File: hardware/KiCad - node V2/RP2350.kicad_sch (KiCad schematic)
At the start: 91 parts, among them J3 USB_C_Receptacle_USB2.0_14P, SW1 BOOTSEL, U1 RP2350A, U2 THVD1450D, U3 ADXL355BEZ, U4 TPS2121RUXR, U5 USBLC6-2SC6, U6 TLV75733PDBV, U7 W25Q128JVS, U8 TPS7A20xxxDBV

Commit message: hardware: 3v3_dig, 1vcore
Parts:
- C19, C20, C21, C22, C25: footprint Capacitor_SMD:C_0603_1608Metric -> Capacitor_SMD:C_0402_1005Metric
- C23, C26: footprint Capacitor_SMD:C_0805_2012Metric -> Capacitor_SMD:C_0603_1608Metric
- R17: footprint Resistor_SMD:R_0201_0603Metric -> Resistor_SMD:R_0402_1005Metric
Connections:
- net USB_VBUS: now also J3.A4 (VBUS), J3.A9 (VBUS), J3.B4 (VBUS)
- net at U2.1 (RO): now also U1.29 (GPIO18)
- net at U2.4 (DI): now also U1.31 (GPIO19)
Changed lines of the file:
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@@
 	)
 	(junction
+		(at 186.69 241.3)
+		(diameter 0)
+		(color 0 0 0 0)
+	)
+	(junction
 		(at 137.16 228.6)
 		(diameter 0)
@@
 	)
 	(junction
+		(at 173.99 232.41)
+		(diameter 0)
+		(color 0 0 0 0)
+	)
+	(junction
 		(at 100.33 113.03)
 		(diameter 0)
@@
 	)
 	(junction
+		(at 173.99 241.3)
+		(diameter 0)
+		(color 0 0 0 0)
+	)
+	(junction
 		(at 46.99 237.49)
 		(diameter 0)
@@
 	(wire
 		(pts
+			(xy 186.69 255.27) (xy 186.69 241.3)
+		)
+		(stroke
+			(width 0)
+			(type default)
+		)
+	)
+	(wire
+		(pts
 			(xy 196.85 31.75) (xy 196.85 34.29)
 		)
@@
 	(wire
 		(pts
+			(xy 214.63 78.74) (xy 214.63 88.9)
+		)
+		(stroke
+			(width 0)
+			(type default)
+		)
+	)
+	(wire
+		(pts
 			(xy 201.93 40.64) (xy 198.12 40.64)
 		)
@@
 	(wire
 		(pts
+			(xy 186.69 232.41) (xy 186.69 241.3)
+		)
+		(stroke
+			(width 0)
+			(type default)
+		)
+	)
+	(wire
+		(pts
 			(xy 123.19 76.2) (xy 121.92 76.2)
 		)
@@
 	(wire
 		(pts
-			(xy 121.92 72.39) (xy 168.91 72.39)
+			(xy 121.92 72.39) (xy 217.17 72.39)
 		)
 		(stroke
@@
 	(wire
 		(pts
+			(xy 173.99 232.41) (xy 173.99 241.3)
+		)
+		(stroke
+			(width 0)
+			(type default)
+		)
+	)
+	(wire
+		(pts
 			(xy 52.07 142.24) (xy 52.07 157.48)
 		)
@@
 	(wire
 		(pts
+			(xy 217.17 72.39) (xy 217.17 88.9)
+		)
+		(stroke
+			(width 0)
+			(type default)
+		)
+	)
+	(wire
+		(pts
 			(xy 100.33 133.35) (xy 100.33 135.89)
 		)
@@
 	(wire
 		(pts
-			(xy 121.92 78.74) (xy 171.45 78.74)
+			(xy 121.92 78.74) (xy 214.63 78.74)
 		)
 		(stroke
@@
 	(wire
 		(pts
+			(xy 173.99 241.3) (xy 173.99 255.27)
+		)
+		(stroke
+			(width 0)
+			(type default)
+		)
+	)
+	(wire
+		(pts
 			(xy 181.61 247.65) (xy 181.61 255.27)
 		)
@@
 	(wire
 		(pts
+			(xy 186.69 241.3) (xy 173.99 241.3)
+		)
+		(stroke
+			(width 0)
+			(type default)
+		)
+	)
+	(wire
+		(pts
 			(xy 209.55 142.24) (xy 255.27 142.24)
 		)
@@
 			)
 		)
-		(property "Footprint" "Capacitor_SMD:C_0603_1608Metric"
+		(property "Footprint" "Capacitor_SMD:C_0402_1005Metric"
 			(at 153.67 127 0)
 			(hide yes)
@@
 			)
 		)
-		(property "Footprint" "Capacitor_SMD:C_0805_2012Metric"
+		(property "Footprint" "Capacitor_SMD:C_0603_1608Metric"
 			(at 134.62 114.3 0)
 			(hide yes)
@@
 			)
 		)
-		(property "Footprint" "Capacitor_SMD:C_0603_1608Metric"
+		(property "Footprint" "Capacitor_SMD:C_0402_1005Metric"
 			(at 158.75 129.54 0)
 			(hide yes)
@@
 			)
 		)
-		(property "Footprint" "Capacitor_SMD:C_0603_1608Metric"
+		(property "Footprint" "Capacitor_SMD:C_0402_1005Metric"
 			(at 154.94 87.63 0)
 			(hide yes)
@@
 			)
 		)
-		(property "Footprint" "Capacitor_SMD:C_0603_1608Metric"
+		(property "Footprint" "Capacitor_SMD:C_0402_1005Metric"
 			(at 142.24 119.38 0)
 			(hide yes)
@@
 			)
 		)
-		(property "Footprint" "Capacitor_SMD:C_0805_2012Metric"
+		(property "Footprint" "Capacitor_SMD:C_0603_1608Metric"
 			(at 148.59 87.63 0)
 			(hide yes)
@@
 			)
 		)
-		(property "Footprint" "Resistor_SMD:R_0201_0603Metric"
+		(property "Footprint" "Resistor_SMD:R_0402_1005Metric"
 			(at 144.78 135.89 0)
 			(hide yes)
@@
 			)
 		)
-		(property "Footprint" "Capacitor_SMD:C_0603_1608Metric"
+		(property "Footprint" "Capacitor_SMD:C_0402_1005Metric"
 			(at 149.86 121.92 0)
 			(hide yes)

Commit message: hardware: new layout
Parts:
- removed R25, R26, R28, R29: 33ohm, Resistor_SMD:R_0603_1608Metric, symbol Device:R_Small
- C30, C34, C35, C37: footprint Capacitor_SMD:C_0603_1608Metric -> Capacitor_SMD:C_0402_1005Metric
- C36: footprint Capacitor_SMD:C_0805_2012Metric -> Capacitor_SMD:C_0603_1608Metric
- R23, R24, R27: footprint Resistor_SMD:R_0603_1608Metric -> Resistor_SMD:R_0402_1005Metric
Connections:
- net GND: now also J_OUT1.2 (GND)
- net SHIELD: now also J_OUT1.5 (SHIELD)
- net at U2.1 (RO): now also U1.27 (GPIO16); no longer U1.29 (GPIO18)
- net at R22.2, U2.2 (~{RE}), U2.3 (DE): now also U1.29 (GPIO18); no longer U1.4 (GPIO2)
- net at U2.4 (DI): now also U1.28 (GPIO17); no longer U1.31 (GPIO19)
- net ADXL_MISO: now reaches U3.4 (MISO/ASEL)
- net ADXL_MISO: now also U1.12 (GPIO8)
- net ADXL_CS: now reaches R27.2, U3.1 (*CS/SCL)
- net ADXL_CS: now also U1.13 (GPIO9)
- net ADXL_INT1: now reaches U3.12 (INT1)
- net ADXL_INT1: now also U1.18 (GPIO14); no longer U1.17 (GPIO13)
- net ADXL_INT2: now reaches U3.13 (INT2)
- net ADXL_INT2: now also U1.17 (GPIO13); no longer U1.18 (GPIO14)
- net ADXL_DRDY: now reaches U1.16 (GPIO12), U3.14 (DRDY)
- net ADXL_SCLK: now reaches U3.2 (SCLK/VSSIO)
- net ADXL_SCLK: now also U1.14 (GPIO10)
- net ADXL_MOSI: now reaches U3.3 (MOSI/SDA)
- net ADXL_MOSI: now also U1.15 (GPIO11)
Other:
- moved on the sheet: R22, R27

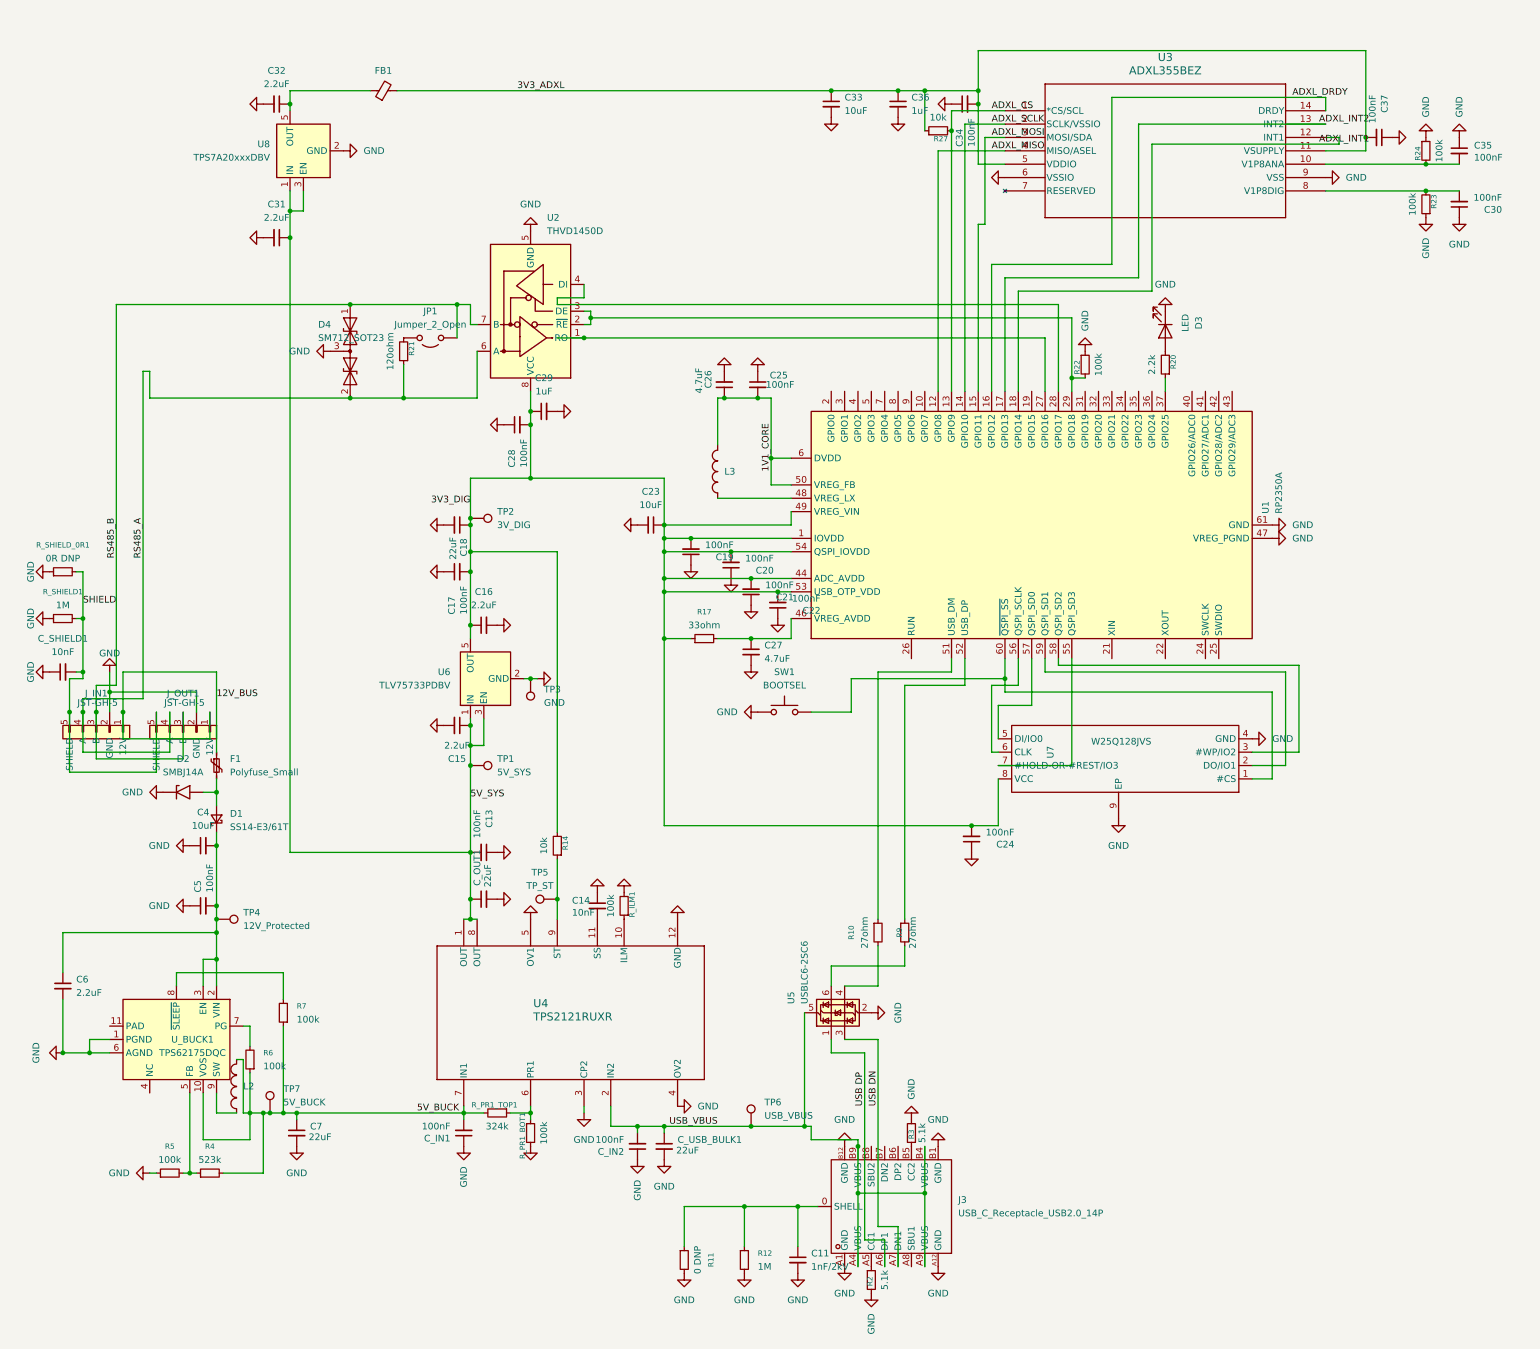
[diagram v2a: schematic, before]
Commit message: hardware: ERC fixes, PWR_FLAG, and net labels
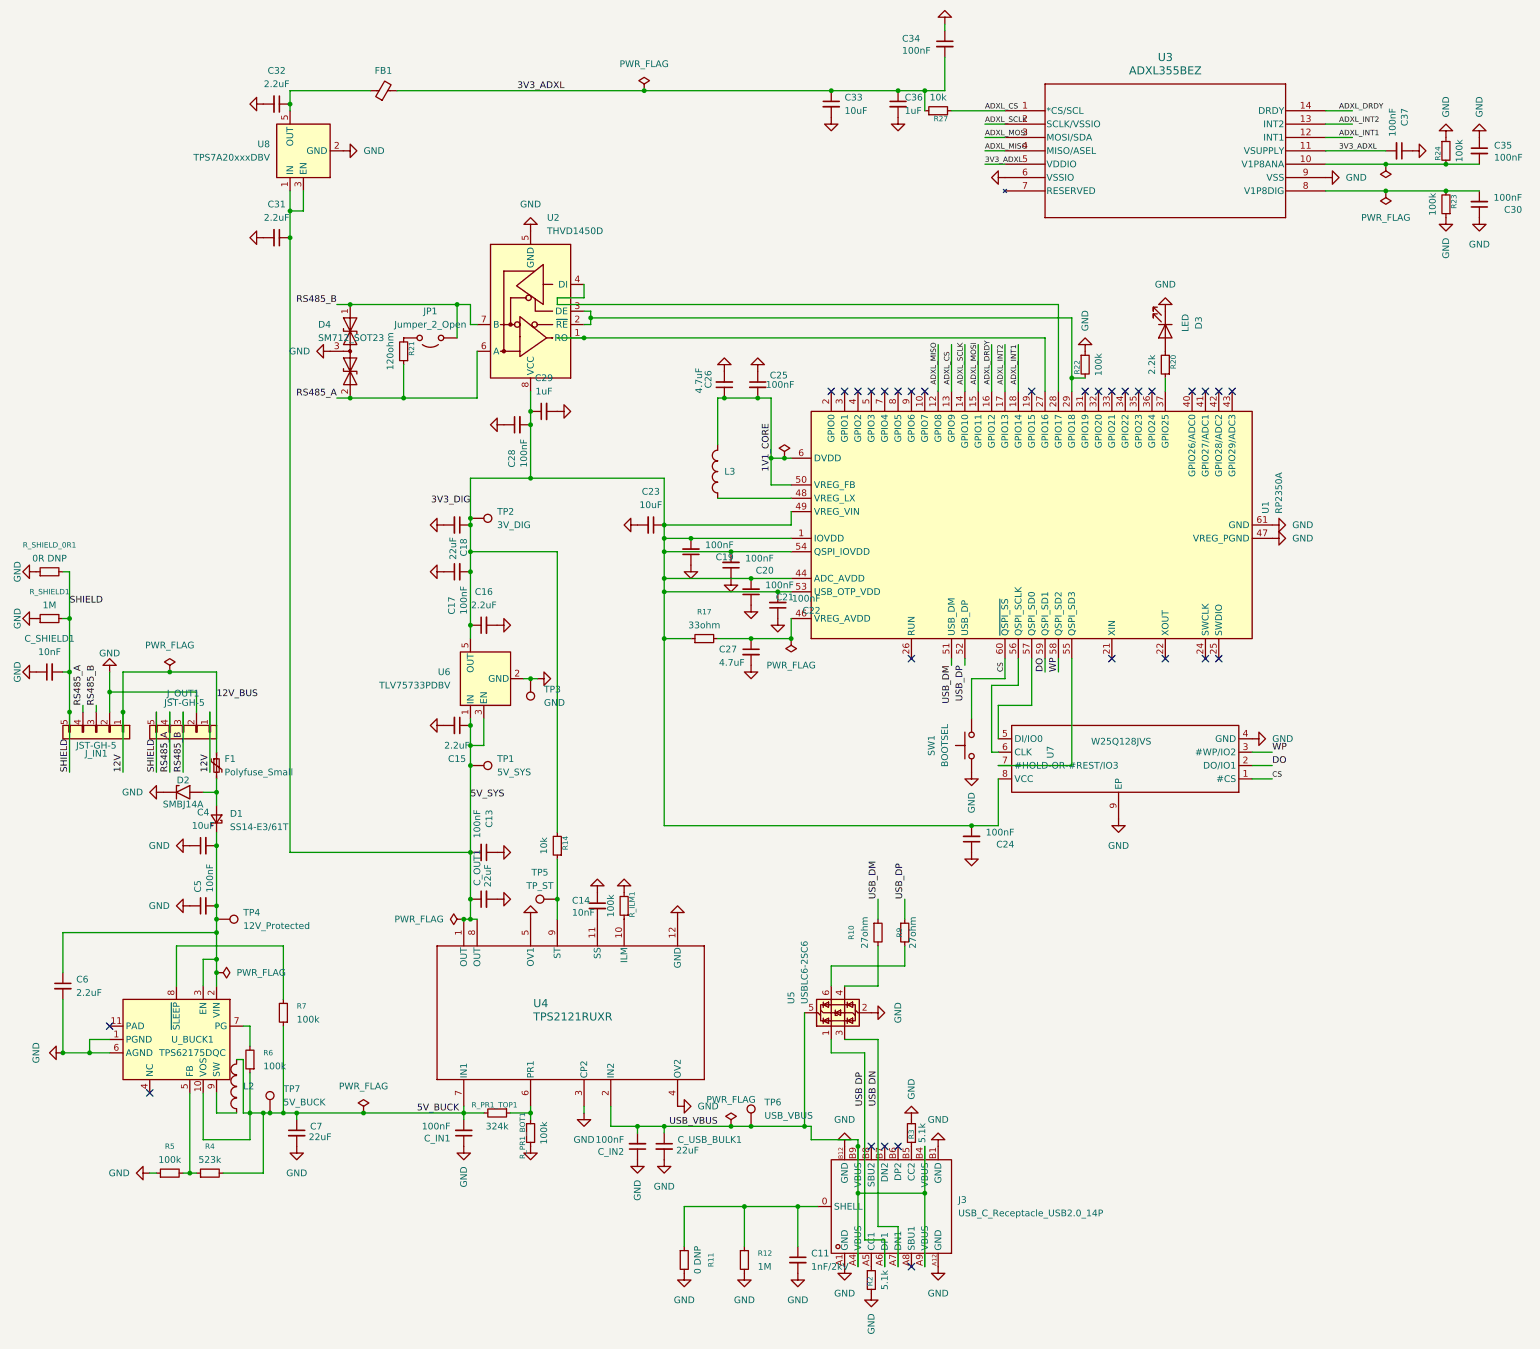
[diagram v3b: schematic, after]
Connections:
- net CS: now reaches SW1.2, U1.60 (~{QSPI_SS}), U7.1 (#CS)
- net DO: now reaches U1.59 (QSPI_SD1), U7.2 (DO/IO1)
- net WP: now reaches U1.58 (QSPI_SD2), U7.3 (#WP/IO2)
- net USB_DP: now reaches R9.1, U1.52 (USB_DP)
- net USB_DM: now reaches R10.1, U1.51 (USB_DM)
- net 12V_BUS renamed 12V
- no-connect marks 0 -> 30
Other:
- moved on the sheet: C30, C34, C35, C37, C_SHIELD1, R23, R24, R27, R_SHIELD1, R_SHIELD_0R1, SW1

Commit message: hardware: layout updates
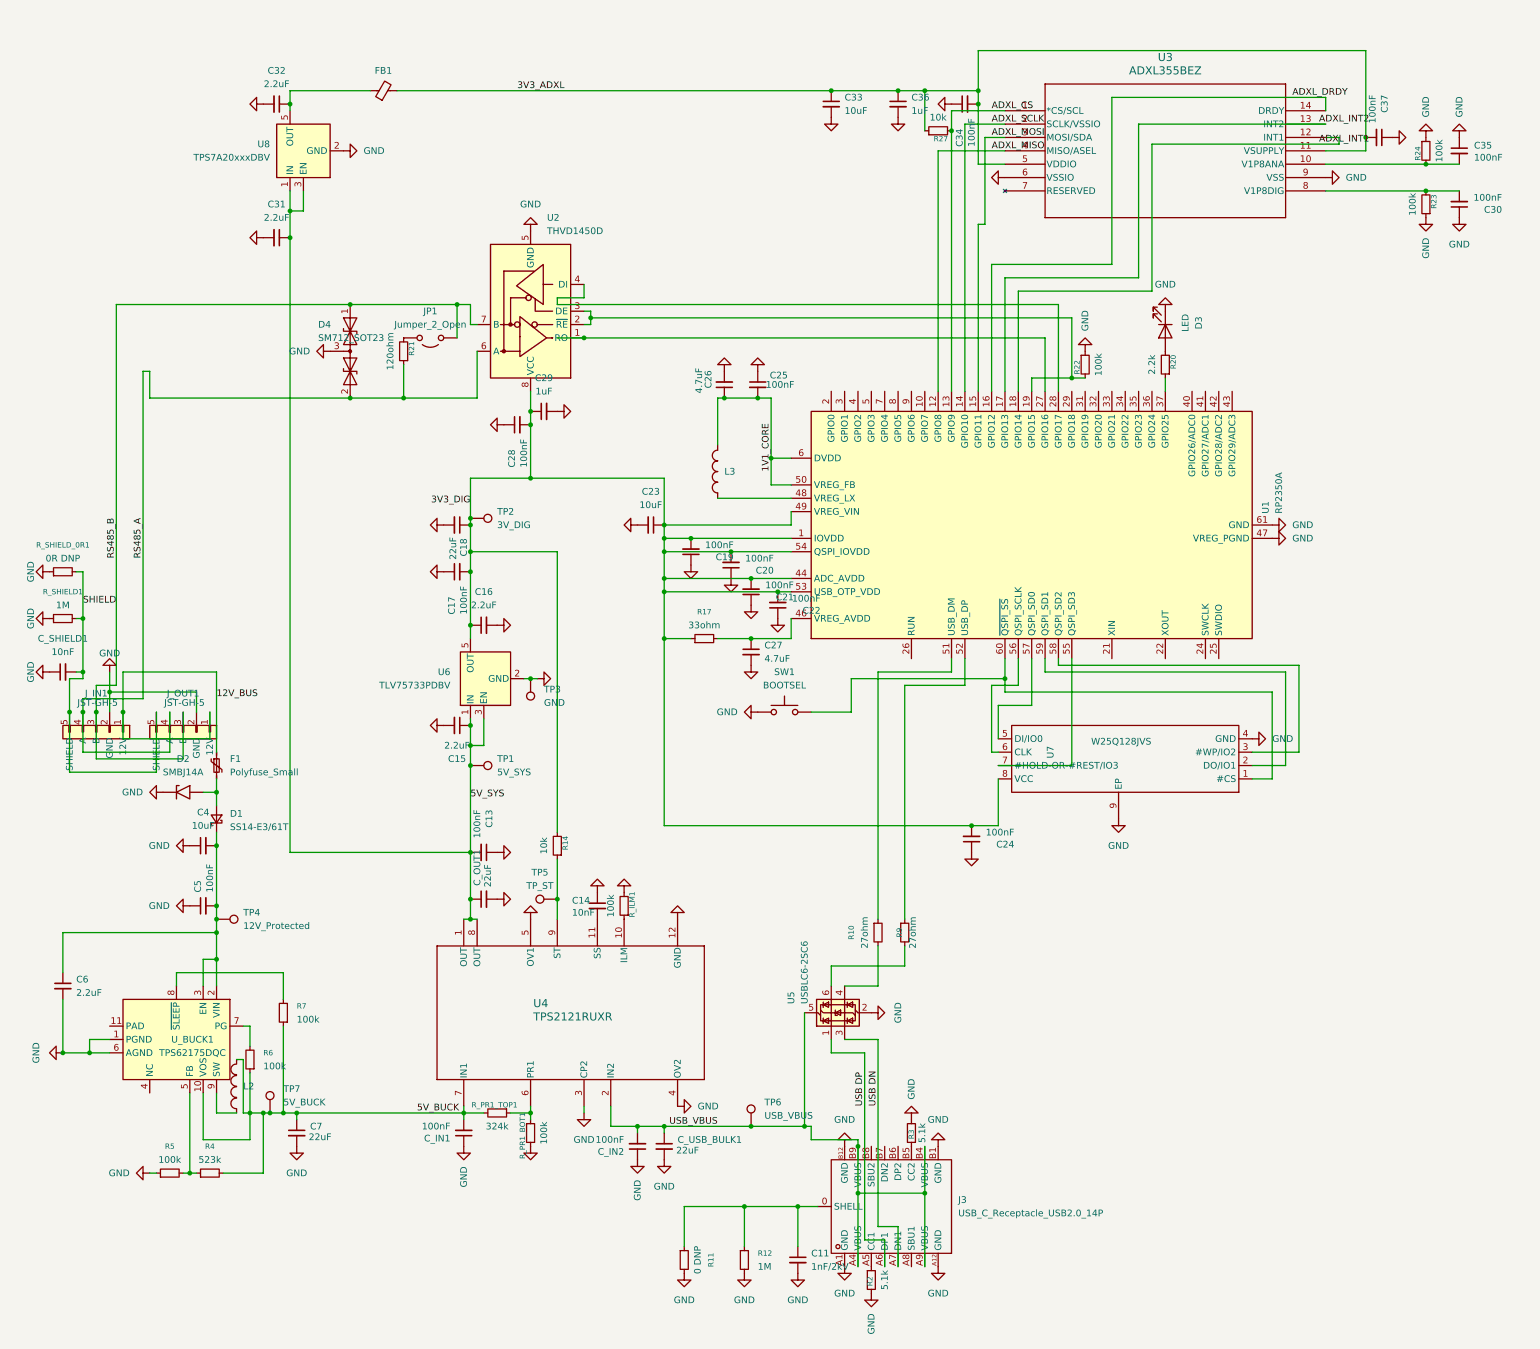
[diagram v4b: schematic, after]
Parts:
- U4: footprint my_footprints:RUX0012A -> footprints:TPS2121RUXR-VQFN-HR-12_L2.5-W2.0-P0.50-BL
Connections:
- net at R22.2, U2.2 (~{RE}), U2.3 (DE): now also U1.19 (GPIO15); no longer U1.29 (GPIO18)
- net 12V renamed 12V_BUS
- net CS: no longer names the net of SW1.2, U1.60 (~{QSPI_SS}), U7.1 (#CS)
- net DO: no longer names the net of U1.59 (QSPI_SD1), U7.2 (DO/IO1)
- net USB_DM: no longer names the net of R10.1, U1.51 (USB_DM)
- net USB_DP: no longer names the net of R9.1, U1.52 (USB_DP)
- net WP: no longer names the net of U1.58 (QSPI_SD2), U7.3 (#WP/IO2)
- no-connect marks 30 -> 0
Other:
- moved on the sheet: C30, C34, C35, C37, C_SHIELD1, R23, R24, R27, R_SHIELD1, R_SHIELD_0R1, SW1
